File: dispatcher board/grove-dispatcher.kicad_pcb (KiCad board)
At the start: 2 copper layers, 156.8 x 75.6 mm, 71 parts, among them P1 CONN_01X12, P10 CONN_01X06, P11 CONN_01X06, P12 CONN_01X06, P13 CONN_01X06, P14 CONN_01X06, P15 CONN_01X06, P16 CONN_01X06, P17 CONN_01X06, P2 CONN_01X06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

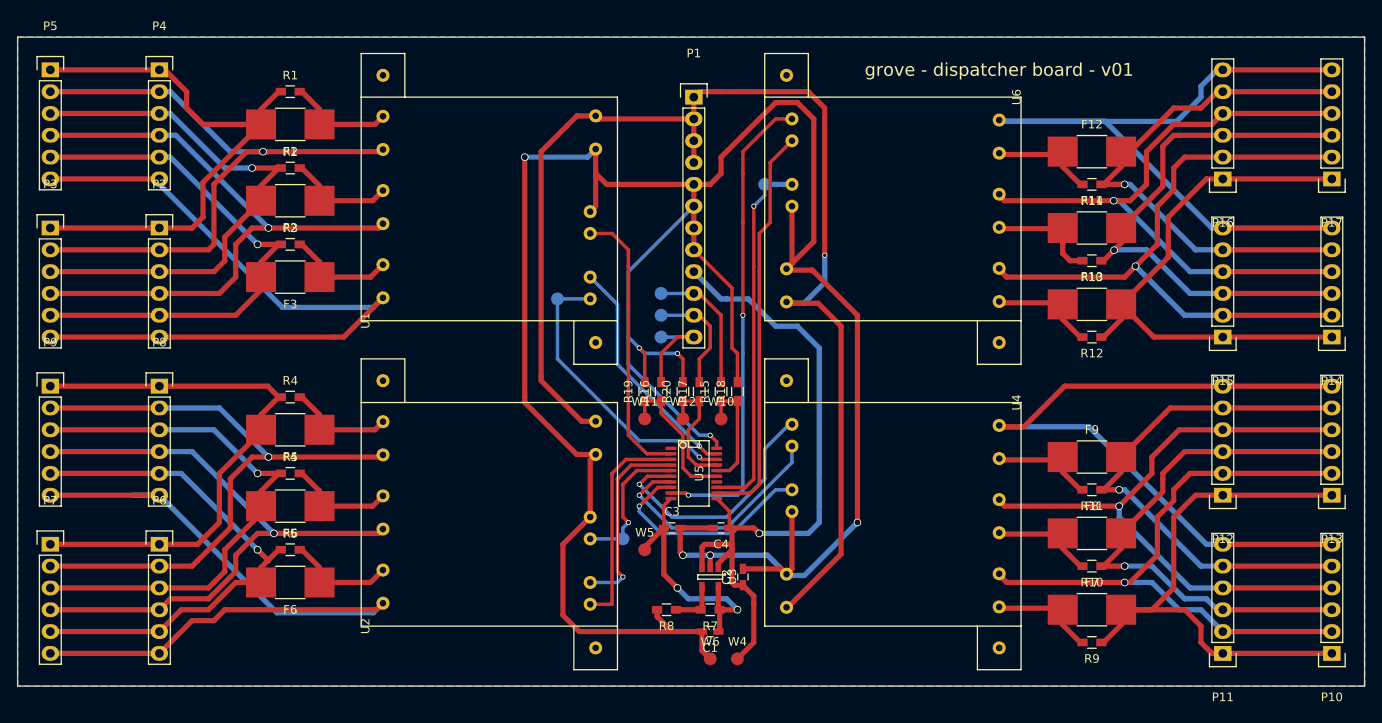
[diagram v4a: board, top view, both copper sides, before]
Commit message: Re add mounting holes
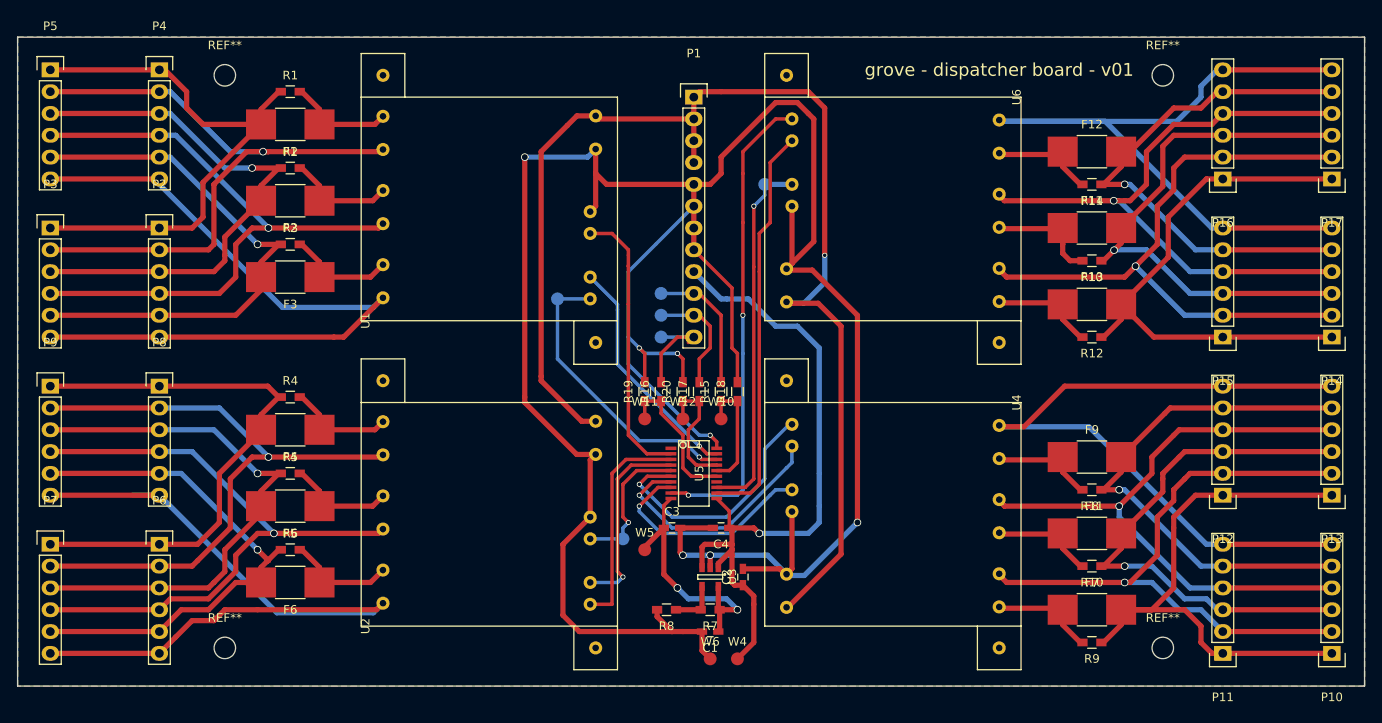
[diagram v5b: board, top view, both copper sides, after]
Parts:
- added REF**: MountingHole_2.5mm, Mounting_Holes:MountingHole_2.5mm, F.Cu at (85.7, 61.6)
- added REF**: MountingHole_2.5mm, Mounting_Holes:MountingHole_2.5mm, F.Cu at (85.7, 128.3)
- added REF**: MountingHole_2.5mm, Mounting_Holes:MountingHole_2.5mm, F.Cu at (194.9, 61.6)
- added REF**: MountingHole_2.5mm, Mounting_Holes:MountingHole_2.5mm, F.Cu at (194.9, 128.3)
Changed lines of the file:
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@@
     (tracks 673)
     (zones 0)
-    (modules 71)
+    (modules 75)
     (nets 60)
   )
@@
   )
   (setup
-    (last_trace_width 0.6096)
+    (last_trace_width 0.25)
     (user_trace_width 0.2032)
     (user_trace_width 0.254)
@@
     (pad_to_mask_clearance 0)
     (aux_axis_origin 0 0)
-    (grid_origin 135.255 81.28)
+    (grid_origin 154.94 53.975)
     (visible_elements FFFFFF7F)
     (pcbplotparams
@@
     (pad 11 thru_hole circle (at 23.368 -2.54 270) (size 1.524 1.524) (drill 0.762) (layers *.Cu *.Mask F.SilkS)
       (net 43 "Net-(P14-Pad6)"))
+  )
+  (module Mounting_Holes:MountingHole_2.5mm (layer F.Cu)
+    (at 85.725 61.595)
+    (descr "Mounting Hole 2.5mm, no annular")
+    (tags "mounting hole 2.5mm no annular")
+    (fp_text reference REF** (at 0 -3.5) (layer F.SilkS)
+      (effects (font (size 1 1) (thickness 0.15)))
+    )
+    (fp_text value MountingHole_2.5mm (at 0 3.5) (layer F.Fab)
+      (effects (font (size 1 1) (thickness 0.15)))
+    )
+    (fp_circle (center 0 0) (end 2.5 0) (layer Cmts.User) (width 0.15))
+    (fp_circle (center 0 0) (end 2.75 0) (layer F.CrtYd) (width 0.05))
+    (pad 1 np_thru_hole circle (at 0 0) (size 2.5 2.5) (drill 2.5) (layers *.Cu *.Mask F.SilkS))
+  )
+  (module Mounting_Holes:MountingHole_2.5mm (layer F.Cu)
+    (at 85.725 128.27)
+    (descr "Mounting Hole 2.5mm, no annular")
+    (tags "mounting hole 2.5mm no annular")
+    (fp_text reference REF** (at 0 -3.5) (layer F.SilkS)
+      (effects (font (size 1 1) (thickness 0.15)))
+    )
+    (fp_text value MountingHole_2.5mm (at 0 3.5) (layer F.Fab)
+      (effects (font (size 1 1) (thickness 0.15)))
+    )
+    (fp_circle (center 0 0) (end 2.5 0) (layer Cmts.User) (width 0.15))
+    (fp_circle (center 0 0) (end 2.75 0) (layer F.CrtYd) (width 0.05))
+    (pad 1 np_thru_hole circle (at 0 0) (size 2.5 2.5) (drill 2.5) (layers *.Cu *.Mask F.SilkS))
+  )
+  (module Mounting_Holes:MountingHole_2.5mm (layer F.Cu)
+    (at 194.945 61.595)
+    (descr "Mounting Hole 2.5mm, no annular")
+    (tags "mounting hole 2.5mm no annular")
+    (fp_text reference REF** (at 0 -3.5) (layer F.SilkS)
+      (effects (font (size 1 1) (thickness 0.15)))
+    )
+    (fp_text value MountingHole_2.5mm (at 0 3.5) (layer F.Fab)
+      (effects (font (size 1 1) (thickness 0.15)))
+    )
+    (fp_circle (center 0 0) (end 2.5 0) (layer Cmts.User) (width 0.15))
+    (fp_circle (center 0 0) (end 2.75 0) (layer F.CrtYd) (width 0.05))
+    (pad 1 np_thru_hole circle (at 0 0) (size 2.5 2.5) (drill 2.5) (layers *.Cu *.Mask F.SilkS))
+  )
+  (module Mounting_Holes:MountingHole_2.5mm (layer F.Cu)
+    (at 194.945 128.27)
+    (descr "Mounting Hole 2.5mm, no annular")
+    (tags "mounting hole 2.5mm no annular")
+    (fp_text reference REF** (at 0 -3.5) (layer F.SilkS)
+      (effects (font (size 1 1) (thickness 0.15)))
+    )
+    (fp_text value MountingHole_2.5mm (at 0 3.5) (layer F.Fab)
+      (effects (font (size 1 1) (thickness 0.15)))
+    )
+    (fp_circle (center 0 0) (end 2.5 0) (layer Cmts.User) (width 0.15))
+    (fp_circle (center 0 0) (end 2.75 0) (layer F.CrtYd) (width 0.05))
+    (pad 1 np_thru_hole circle (at 0 0) (size 2.5 2.5) (drill 2.5) (layers *.Cu *.Mask F.SilkS))
   )
   (gr_line (start 61.595 132.715) (end 218.44 132.715) (angle 90) (layer Edge.Cuts) (width 0.1))
@@
   (segment (start 128.905 66.3194) (end 126.7206 66.3194) (width 0.6096) (layer F.Cu) (net 25))
   (segment (start 127.2794 101.8794) (end 122.555 97.155) (width 0.6096) (layer F.Cu) (net 25))
-  (segment (start 127.2794 101.8794) (end 128.905 101.8794) (width 0.6096) (layer F.Cu) (net 25) (status 800000))
+  (segment (start 127.2794 101.8794) (end 128.905 101.8794) (width 0.6096) (layer F.Cu) (net 25))
   (segment (start 140.335 66.675) (end 129.2606 66.675) (width 0.6096) (layer F.Cu) (net 25))
   (segment (start 129.2606 66.675) (end 128.905 66.3194) (width 0.6096) (layer F.Cu) (net 25))
@@
   (segment (start 140.335 69.215) (end 140.335 66.675) (width 0.6096) (layer F.Cu) (net 25) (status 30))
   (segment (start 140.335 64.135) (end 140.335 66.675) (width 0.6096) (layer F.Cu) (net 25) (status 30))
-  (segment (start 128.905 105.7402) (end 126.6952 105.7402) (width 0.6096) (layer F.Cu) (net 26) (status 400000))
+  (segment (start 128.905 105.7402) (end 126.6952 105.7402) (width 0.6096) (layer F.Cu) (net 26))
   (segment (start 127.9652 71.12) (end 128.905 70.1802) (width 0.6096) (layer B.Cu) (net 26))
   (via (at 120.65 71.12) (size 0.889) (drill 0.6858) (layers F.Cu B.Cu) (net 26))
@@
   (segment (start 120.65 99.695) (end 120.65 99.06) (width 0.6096) (layer F.Cu) (net 26))
   (segment (start 126.6952 105.7402) (end 120.65 99.695) (width 0.6096) (layer F.Cu) (net 26))
-  (segment (start 128.27 113.03) (end 128.27 106.3752) (width 0.6096) (layer F.Cu) (net 26) (status 400000))
-  (segment (start 128.27 106.3752) (end 128.905 105.7402) (width 0.6096) (layer F.Cu) (net 26) (status 800000))
+  (segment (start 128.27 113.03) (end 128.27 106.3752) (width 0.6096) (layer F.Cu) (net 26))
+  (segment (start 128.27 106.3752) (end 128.905 105.7402) (width 0.6096) (layer F.Cu) (net 26))
   (segment (start 125.095 124.46) (end 125.095 116.205) (width 0.6096) (layer F.Cu) (net 26))
   (segment (start 127 126.365) (end 125.095 124.46) (width 0.6096) (layer F.Cu) (net 26))
   (segment (start 137.795 126.365) (end 127 126.365) (width 0.6096) (layer F.Cu) (net 26))
-  (segment (start 125.095 116.205) (end 128.27 113.03) (width 0.6096) (layer F.Cu) (net 26) (status 800000))
+  (segment (start 125.095 116.205) (end 128.27 113.03) (width 0.6096) (layer F.Cu) (net 26))
   (segment (start 140.335 74.295) (end 130.175 74.295) (width 0.6096) (layer F.Cu) (net 26))
   (segment (start 130.175 74.295) (end 128.905 73.025) (width 0.6096) (layer F.Cu) (net 26))

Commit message: Fill zones, merge segements and run DRC
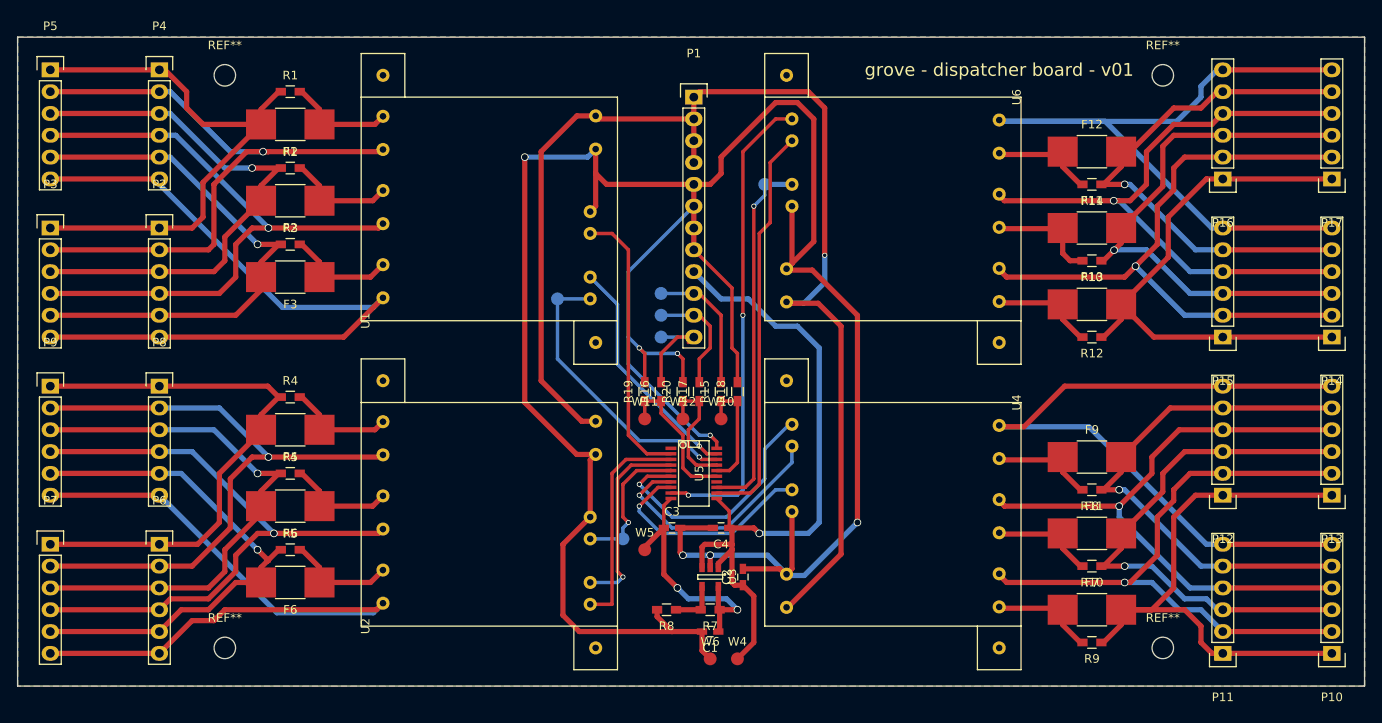
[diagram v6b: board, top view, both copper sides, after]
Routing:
- net Net-(P6-Pad6): track 89.2 -> 86.0 mm

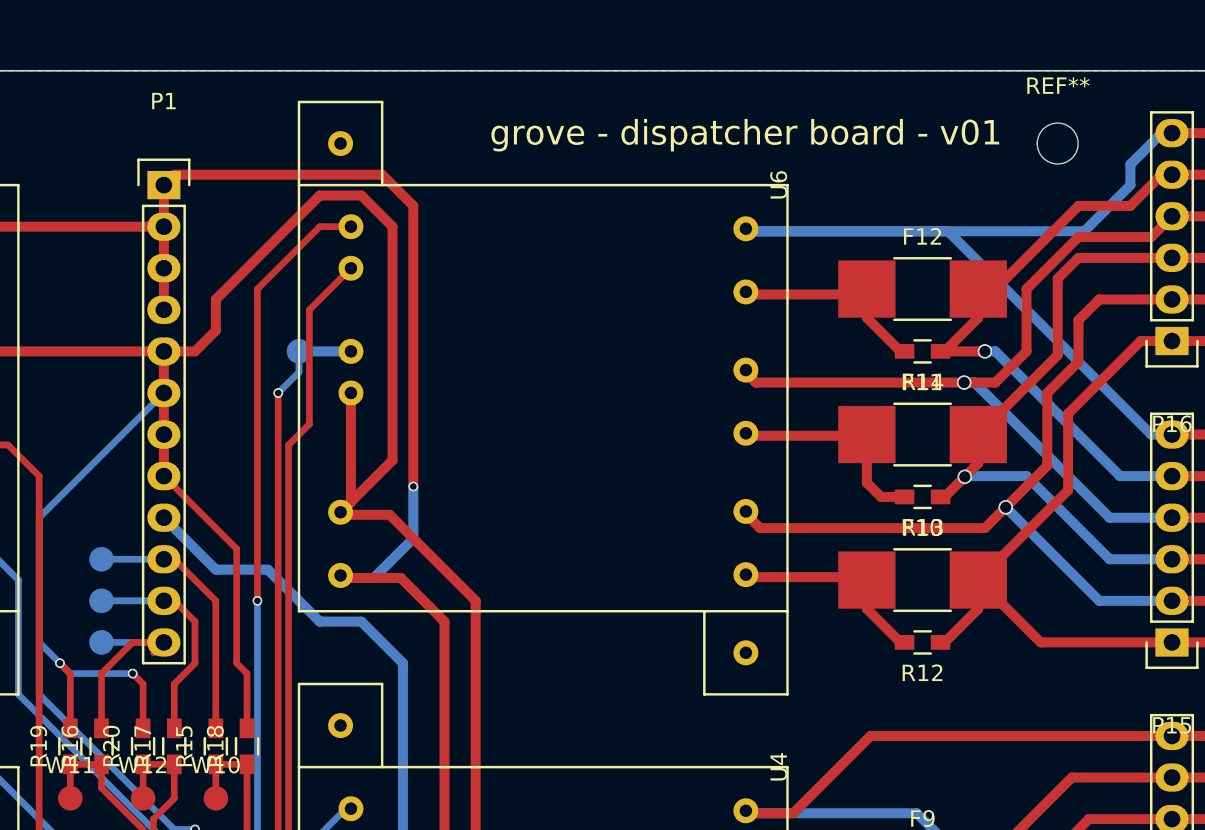
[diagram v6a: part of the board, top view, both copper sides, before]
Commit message: Fix changed connector ordering
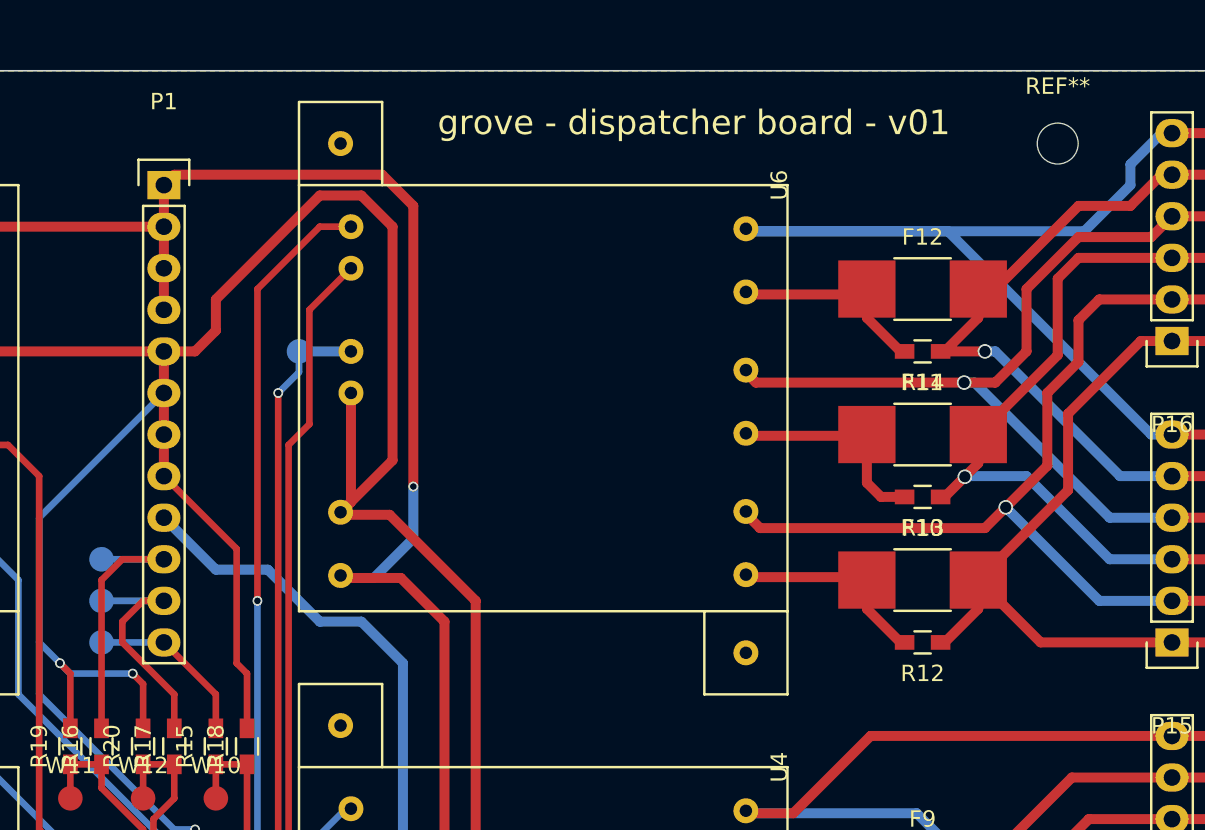
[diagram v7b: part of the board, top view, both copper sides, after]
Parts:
- moved W1 5.08 mm to (136.5, 92.1)
- moved W3 5.08 mm to (136.5, 87.0)
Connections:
- P1 pad 10: /SCLK_5V -> /CS_5V
- P1 pad 12: /CS_5V -> /SCLK_5V
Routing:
- net /SCLK_5V: track 15.8 -> 10.4 mm
- net /CS_5V: track 12.7 -> 17.8 mm
- net /MOSI_5V: track 13.3 -> 15.3 mm
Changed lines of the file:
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@@
     (links 204)
     (no_connects 0)
-    (area 60.296667 54.735 219.738334 134.98)
+    (area 61.544999 57.099999 218.490001 132.765001)
     (thickness 1.6)
     (drawings 5)
@@
   )
   (setup
-    (last_trace_width 0.25)
+    (last_trace_width 0.4064)
     (user_trace_width 0.2032)
     (user_trace_width 0.254)
@@
       (net 35 +5V))
     (pad 10 thru_hole oval (at 0 22.86) (size 2.032 1.7272) (drill 1.016) (layers *.Cu *.Mask F.SilkS)
-      (net 36 /SCLK_5V))
+      (net 38 /CS_5V))
     (pad 11 thru_hole oval (at 0 25.4) (size 2.032 1.7272) (drill 1.016) (layers *.Cu *.Mask F.SilkS)
       (net 37 /MOSI_5V))
     (pad 12 thru_hole oval (at 0 27.94) (size 2.032 1.7272) (drill 1.016) (layers *.Cu *.Mask F.SilkS)
-      (net 38 /CS_5V))
+      (net 36 /SCLK_5V))
     (model Pin_Headers.3dshapes/Pin_Header_Straight_1x12.wrl
       (at (xyz 0 -0.55 0))
@@
   )
   (module Measurement_Points:Measurement_Point_Round-SMD-Pad_Small (layer B.Cu)
-    (at 136.525 86.995)
+    (at 136.525 92.075)
     (descr "Mesurement Point, Round, SMD Pad, DM 1.5mm,")
     (tags "Mesurement Point Round SMD Pad 1.5mm")
@@
   )
   (module Measurement_Points:Measurement_Point_Round-SMD-Pad_Small (layer B.Cu)
-    (at 136.525 92.075)
+    (at 136.525 86.995)
     (descr "Mesurement Point, Round, SMD Pad, DM 1.5mm,")
     (tags "Mesurement Point Round SMD Pad 1.5mm")
@@
   (gr_line (start 218.44 57.15) (end 61.595 57.15) (angle 90) (layer Edge.Cuts) (width 0.1))
   (gr_line (start 218.44 132.715) (end 218.44 57.15) (angle 90) (layer Edge.Cuts) (width 0.1))
-  (gr_text "grove - dispatcher board - v01" (at 175.895 60.96) (layer F.SilkS)
+  (gr_text "grove - dispatcher board - v01" (at 172.72 60.325) (layer F.SilkS)
     (effects (font (size 1.5 1.5) (thickness 0.3)))
   )
@@
   (segment (start 144.46 114.3) (end 144.46 112.329) (width 0.4064) (layer F.Cu) (net 35) (status 10))
   (segment (start 144.46 112.329) (end 143.002 110.871) (width 0.4064) (layer F.Cu) (net 35) (status 20))
-  (segment (start 143.51 97.325) (end 143.51 89.535) (width 0.4064) (layer F.Cu) (net 36) (status 10))
-  (segment (start 143.51 89.535) (end 140.97 86.995) (width 0.4064) (layer F.Cu) (net 36) (status 20))
-  (segment (start 140.97 86.995) (end 140.335 86.995) (width 0.4064) (layer F.Cu) (net 36) (status 30))
-  (segment (start 140.335 86.995) (end 136.525 86.995) (width 0.4064) (layer B.Cu) (net 36) (status 30))
-  (segment (start 140.97 97.325) (end 140.97 94.615) (width 0.4064) (layer F.Cu) (net 37) (status 10))
-  (segment (start 142.24 90.805) (end 140.97 89.535) (width 0.4064) (layer F.Cu) (net 37) (status 20))
-  (segment (start 142.24 93.345) (end 142.24 90.805) (width 0.4064) (layer F.Cu) (net 37))
-  (segment (start 140.97 94.615) (end 142.24 93.345) (width 0.4064) (layer F.Cu) (net 37))
+  (segment (start 143.51 97.325) (end 143.51 95.25) (width 0.4064) (layer F.Cu) (net 36))
+  (segment (start 143.51 95.25) (end 140.335 92.075) (width 0.4064) (layer F.Cu) (net 36))
+  (segment (start 140.335 92.075) (end 136.525 92.075) (width 0.4064) (layer B.Cu) (net 36))
+  (segment (start 140.97 97.325) (end 140.97 95.25) (width 0.4064) (layer F.Cu) (net 37))
+  (segment (start 139.065 89.535) (end 140.335 89.535) (width 0.4064) (layer F.Cu) (net 37))
+  (segment (start 137.795 90.805) (end 139.065 89.535) (width 0.4064) (layer F.Cu) (net 37))
+  (segment (start 137.795 92.075) (end 137.795 90.805) (width 0.4064) (layer F.Cu) (net 37))
+  (segment (start 140.97 95.25) (end 137.795 92.075) (width 0.4064) (layer F.Cu) (net 37))
   (segment (start 140.97 89.535) (end 140.335 89.535) (width 0.4064) (layer F.Cu) (net 37) (status 30))
   (segment (start 140.335 89.535) (end 136.525 89.535) (width 0.4064) (layer B.Cu) (net 37) (status 30))
-  (segment (start 140.335 92.075) (end 138.43 92.075) (width 0.4064) (layer F.Cu) (net 38) (status 10))
-  (segment (start 136.525 93.98) (end 136.525 97.325) (width 0.4064) (layer F.Cu) (net 38) (status 20))
-  (segment (start 138.43 92.075) (end 136.525 93.98) (width 0.4064) (layer F.Cu) (net 38))
-  (segment (start 140.335 92.075) (end 136.525 92.075) (width 0.4064) (layer B.Cu) (net 38) (status 30))
-  (segment (start 139.7 92.71) (end 140.335 92.075) (width 0.4064) (layer F.Cu) (net 38) (status 30))
+  (segment (start 136.525 97.325) (end 136.525 88.265) (width 0.4064) (layer F.Cu) (net 38))
+  (segment (start 137.795 86.995) (end 140.335 86.995) (width 0.4064) (layer F.Cu) (net 38))
+  (segment (start 136.525 88.265) (end 137.795 86.995) (width 0.4064) (layer F.Cu) (net 38))
+  (segment (start 140.335 86.995) (end 136.525 86.995) (width 0.4064) (layer B.Cu) (net 38))
+  (segment (start 140.97 86.995) (end 140.335 86.995) (width 0.4064) (layer F.Cu) (net 38) (status 30))
   (segment (start 91.44 114.935) (end 103.632 114.935) (width 0.6096) (layer F.Cu) (net 39) (status 20))
   (segment (start 103.632 114.935) (end 104.14 114.427) (width 0.6096) (layer F.Cu) (net 39) (status 30))
